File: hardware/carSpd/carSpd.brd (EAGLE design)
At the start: 160 x 100 mm, 0 parts

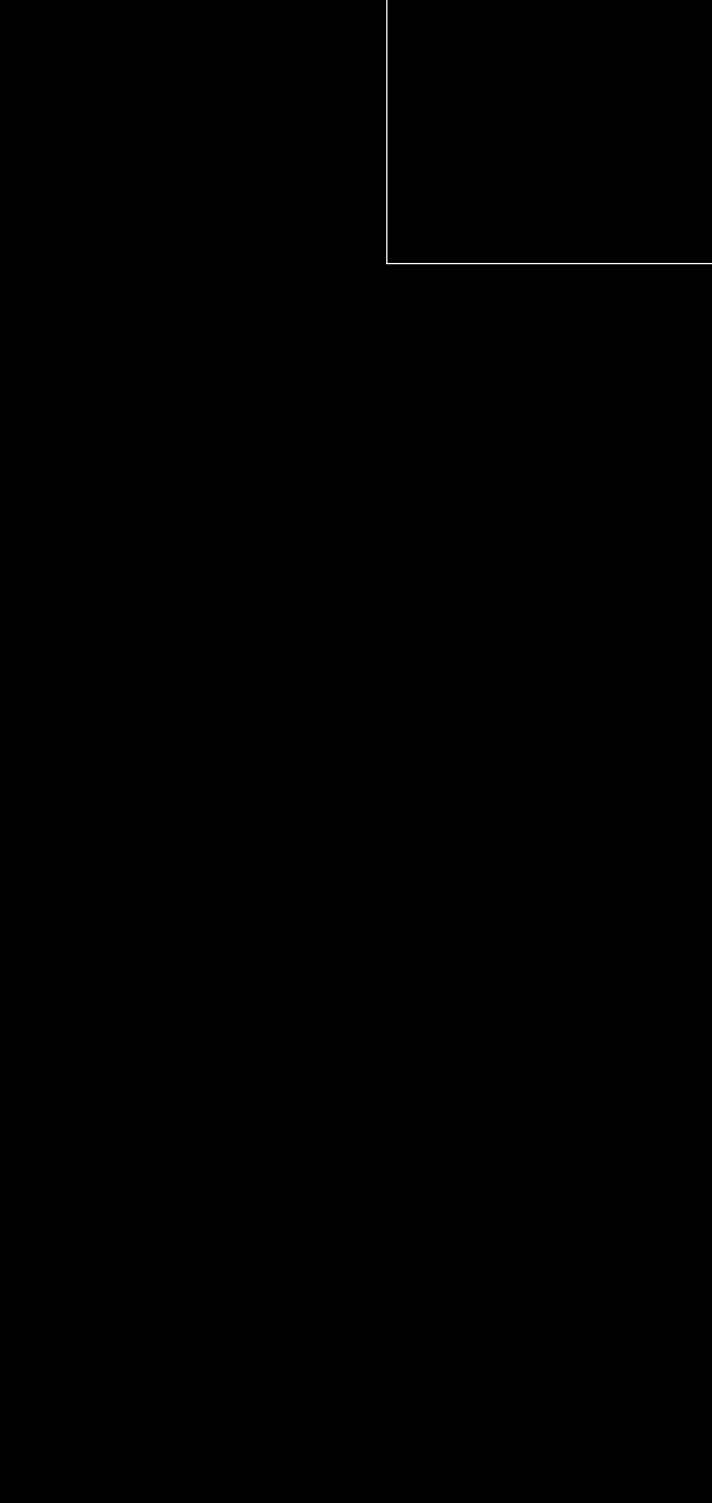
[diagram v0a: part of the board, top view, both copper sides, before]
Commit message: Added power regulator schematics
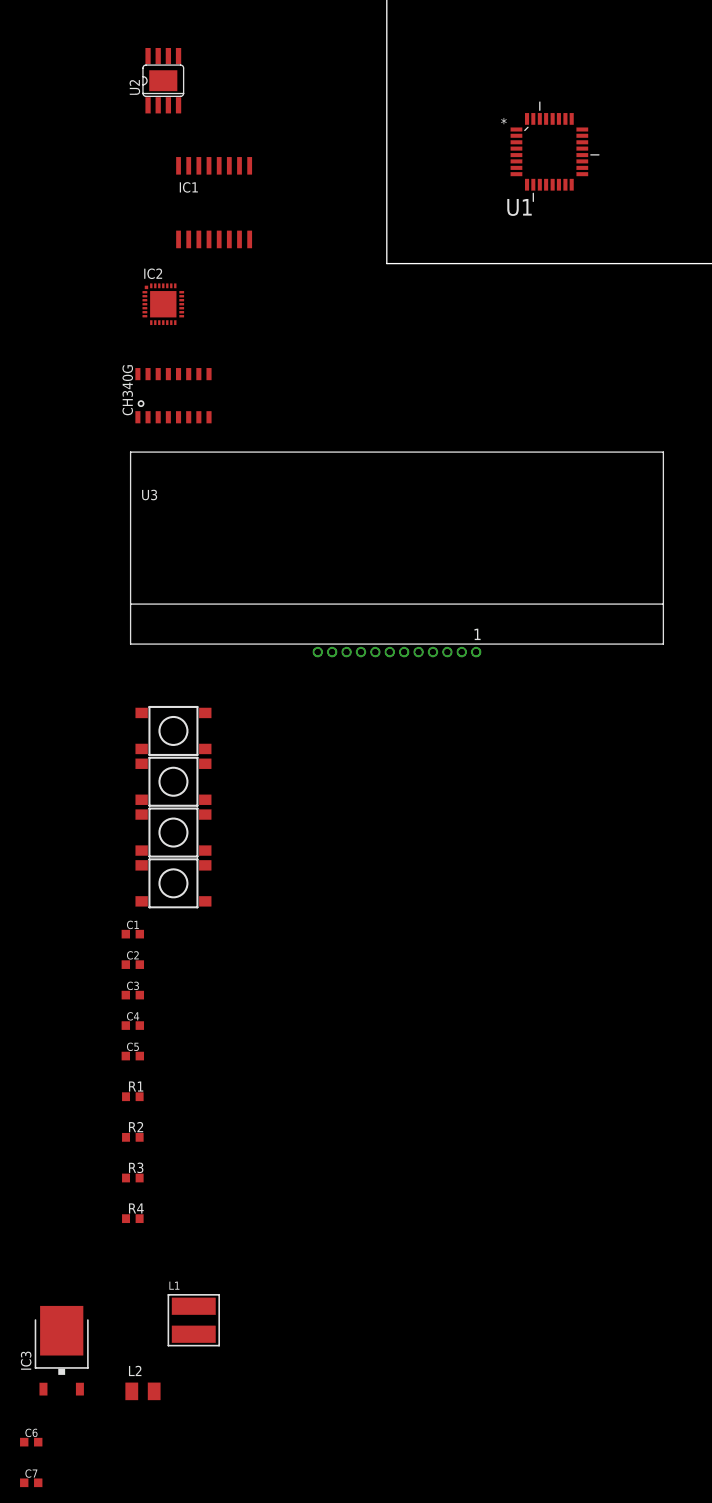
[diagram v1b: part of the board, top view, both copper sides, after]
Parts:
- added C1: 10uf, rcl:C0603K
- added C2: 22uf, rcl:C0603K
- added C3: 3.9nf, rcl:C0603K
- added C4, C7: .1uf, rcl:C0603K
- added C5: 10nf, rcl:C0603K
- added C6: .33uf, rcl:C0603K
- added IC1: DS3231/SO, adafruit:SO16W
- added IC2: CP2102, silabs:MLP28
- added IC3: 7805DT, adafruit:TO252
- added L1: CD54, inductor-sumida:CD54
- added L2: 10uh, rcl:L3225M
- added R1: 10k, rcl:R0603
- added R2: 100k, rcl:R0603
- added R3: 6.8k, rcl:R0603
- added R4: 44.2k, rcl:R0603
- added S1, S2, S3, S4: SWITCH-MOMENTARY-2SMD-4, SparkFun-Electromechanical:TACTILE_SWITCH_TALL
- added U$1: CH340G, ch340g:SOIC16
- added U1: ATMEGA328P-AU, Atmel_By_element14_Batch_1-00:QFP80P900X900X120-32N
- added U2: MP2307, hybridair:SOIC8
- added U3: ERC1602-4, hybridair:ERC1602-4
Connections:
- new net +12V: C1.1, C6.1, IC3.1, R2.2, U2.2
- new net +5V: C2.1, C7.1, IC3.2, L1.1, L2.1, R4.1
- new net AVCC: U1.18
- new net GND: C1.2, C2.2, C4.2, C6.2, C7.2, IC1.13, IC2.3, IC2.EXP, IC2.M, IC3.3, R1.1, R3.1, U2.4, U2.P$1
- new net N$1: C5.2, U2.1
- new net N$2: C5.1, L1.2, L2.2, U2.3
- new net N$3: R1.2, R4.2, U2.5
- new net N$5: C3.2, R3.2
- new net N$6: C3.1, U2.6
- new net N$7: C4.1, U2.8
- new net N$9: R2.1, U2.7
- new net VBAT: IC1.14
- new net VCC: IC1.2, U1.6
- new net VCC_2: U1.4
- new net VDD: IC2.6

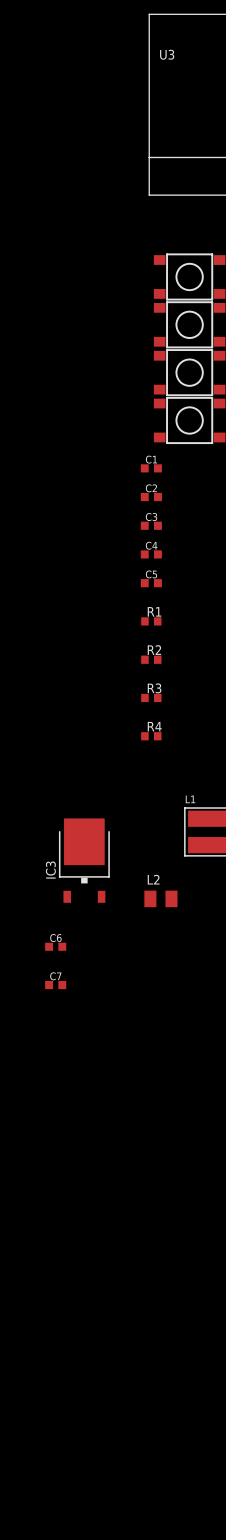
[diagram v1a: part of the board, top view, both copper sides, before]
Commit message: Added USB to serial schematics
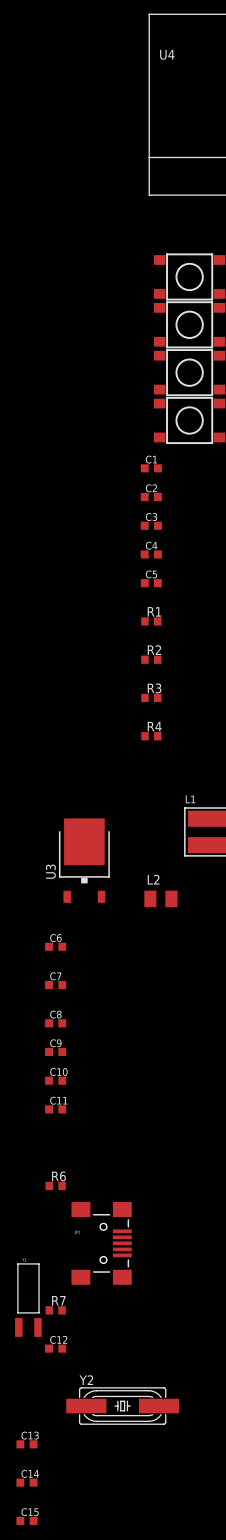
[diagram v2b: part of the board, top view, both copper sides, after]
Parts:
- removed IC3: 7805DT, adafruit:TO252
- added C10, C11, C15, C9: 0.1uf, rcl:C0603K
- added C12: 10nf, rcl:C0603K
- added C13, C14: 18pf, rcl:C0603K
- added C8: 1uf, rcl:C0603K
- added JP1: USBSMD, SparkFun-Connectors:USB-MINIB
- added R6: 4.7k, rcl:R0603
- added R7: 10k, rcl:R0603
- added U4: ERC1602-4, hybridair:ERC1602-4
- added Y1: 12mhz, SparkFun-FreqCtrl:SMD-CYLINDER
- added Y2: (no value), SparkFun-FreqCtrl:HC49UP
- U3: value ERC1602-4 -> 7805DT; device hybridair:ERC1602-4 -> adafruit:TO252
- moved U3 108.7 mm to (-40.6, -135.9)
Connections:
- removed net VDD: IC2.6
- new net D+: IC2.4, U$1.5
- new net D-: IC2.5, U$1.6
- new net N$10: C11.1, IC2.28
- new net N$12: C10.1, IC2.6
- new net N$16: C15.1, U$1.13
- new net N$17: C12.1, U$1.4
- new net N$18: C14.2, U$1.8, Y1.X2, Y2.2
- new net N$19: C13.2, U$1.7, Y1.X1, Y2.1
- new net N$4: IC2.9, R6.1
- new net N$8: IC2.11, R7.2
- new net RST: C11.2, C15.2
- new net RX: IC2.26, U$1.2
- new net TX: IC2.25, U$1.3
- net +12V: now also U3.1; no longer IC3.1
- net +5V: now also C8.1, C9.1, IC2.7, IC2.8, R6.2, U$1.16, U3.2; no longer IC3.2
- net GND: now also C10.2, C12.2, C13.1, C14.1, C8.2, C9.2, R7.1, U$1.1, U3.3; no longer IC3.3
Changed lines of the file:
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@@
 </element>
 <element name="U$1" library="ch340g" package="SOIC16" value="CH340G" x="-26.67" y="-16.51"/>
-<element name="U3" library="hybridair" package="ERC1602-4" value="ERC1602-4" x="1.27" y="-35.56"/>
+<element name="U4" library="hybridair" package="ERC1602-4" value="ERC1602-4" x="1.27" y="-35.56"/>
 <element name="S1" library="SparkFun-Electromechanical" package="TACTILE_SWITCH_TALL" value="SWITCH-MOMENTARY-2SMD-4" x="-26.67" y="-58.42">
 <attribute name="PROD_ID" value="SWCH-11966" x="-26.67" y="-58.42" size="1.778" layer="27" display="off"/>
@@
 <element name="L1" library="inductor-sumida" package="CD54" value="CD54" x="-24.13" y="-132.08"/>
 <element name="L2" library="rcl" package="L3225M" value="10uh" x="-30.48" y="-140.97"/>
-<element name="IC3" library="adafruit" package="TO252" value="7805DT" x="-40.64" y="-135.89"/>
+<element name="U3" library="adafruit" package="TO252" value="7805DT" x="-40.64" y="-135.89"/>
 <element name="C6" library="rcl" package="C0603K" value=".33uf" x="-44.45" y="-147.32"/>
 <element name="C7" library="rcl" package="C0603K" value=".1uf" x="-44.45" y="-152.4"/>
+<element name="C8" library="rcl" package="C0603K" value="1uf" x="-44.45" y="-157.48"/>
+<element name="C9" library="rcl" package="C0603K" value="0.1uf" x="-44.45" y="-161.29"/>
+<element name="C10" library="rcl" package="C0603K" value="0.1uf" x="-44.45" y="-165.1"/>
+<element name="C11" library="rcl" package="C0603K" value="0.1uf" x="-44.45" y="-168.91"/>
+<element name="R6" library="rcl" package="R0603" value="4.7k" x="-44.45" y="-179.07"/>
+<element name="JP1" library="SparkFun-Connectors" package="USB-MINIB" value="USBSMD" x="-38.1" y="-186.69">
+<attribute name="PROD_ID" value="CONN-08193" x="-38.1" y="-186.69" size="1.778" layer="27" display="off"/>
+</element>
+<element name="R7" library="rcl" package="R0603" value="10k" x="-44.45" y="-195.58"/>
+<element name="C12" library="rcl" package="C0603K" value="10nf" x="-44.45" y="-200.66"/>
+<element name="Y1" library="SparkFun-FreqCtrl" package="SMD-CYLINDER" value="12mhz" x="-48.26" y="-198.12"/>
+<element name="Y2" library="SparkFun-FreqCtrl" package="HC49UP" value="" x="-35.56" y="-208.28"/>
+<element name="C13" library="rcl" package="C0603K" value="18pf" x="-48.26" y="-213.36"/>
+<element name="C14" library="rcl" package="C0603K" value="18pf" x="-48.26" y="-218.44"/>
+<element name="C15" library="rcl" package="C0603K" value="0.1uf" x="-48.26" y="-223.52"/>
 </elements>
 <signals>
@@
 <signal name="GND">
 <contactref element="IC1" pad="13"/>
-<contactref element="IC2" pad="3"/>
-<contactref element="IC2" pad="EXP"/>
-<contactref element="IC2" pad="M"/>
 <contactref element="U2" pad="P$1"/>
 <contactref element="U2" pad="4"/>
@@
 <contactref element="C4" pad="2"/>
 <contactref element="C6" pad="2"/>
-<contactref element="IC3" pad="3"/>
+<contactref element="U3" pad="3"/>
 <contactref element="C7" pad="2"/>
+<contactref element="R7" pad="1"/>
+<contactref element="IC2" pad="3"/>
+<contactref element="IC2" pad="EXP"/>
+<contactref element="IC2" pad="M"/>
+<contactref element="C10" pad="2"/>
+<contactref element="C9" pad="2"/>
+<contactref element="C8" pad="2"/>
+<contactref element="U$1" pad="1"/>
+<contactref element="C12" pad="2"/>
+<contactref element="C13" pad="1"/>
+<contactref element="C14" pad="1"/>
+<wire x1="-45.3" y1="-195.58" x2="-43.575" y2="-200.66" width="0" layer="19" extent="1-1"/>
+<wire x1="-49.135" y1="-213.36" x2="-43.575" y2="-200.66" width="0" layer="19" extent="1-1"/>
+<wire x1="-49.135" y1="-218.44" x2="-49.135" y2="-213.36" width="0" layer="19" extent="1-1"/>
+<wire x1="-43.575" y1="-165.1" x2="-45.3" y2="-195.58" width="0" layer="19" extent="1-1"/>
+<wire x1="-43.575" y1="-161.29" x2="-43.575" y2="-165.1" width="0" layer="19" extent="1-1"/>
+<wire x1="-43.575" y1="-157.48" x2="-43.575" y2="-161.29" width="0" layer="19" extent="1-1"/>
+<wire x1="-43.575" y1="-152.4" x2="-43.575" y2="-157.48" width="0" layer="19" extent="1-1"/>
 <wire x1="-43.575" y1="-147.32" x2="-43.575" y2="-152.4" width="0" layer="19" extent="1-1"/>
 <wire x1="-40.64" y1="-133.39" x2="-43.575" y2="-147.32" width="0" layer="19" extent="1-1"/>
@@
 <wire x1="-30.875" y1="-87.63" x2="-30.875" y2="-95.25" width="0" layer="19" extent="1-1"/>
 <wire x1="-30.875" y1="-83.82" x2="-30.875" y2="-87.63" width="0" layer="19" extent="1-1"/>
-<wire x1="-27.94" y1="-5.08" x2="-30.875" y2="-83.82" width="0" layer="19" extent="1-1"/>
+<wire x1="-31.115" y1="-19.205" x2="-30.875" y2="-83.82" width="0" layer="19" extent="1-1"/>
+<wire x1="-27.94" y1="-5.08" x2="-31.115" y2="-19.205" width="0" layer="19" extent="1-1"/>
 <wire x1="-30.24" y1="-4.58" x2="-27.94" y2="-5.08" width="0" layer="19" extent="1-1"/>
 <wire x1="-30.0425" y1="-2.9775" x2="-30.24" y2="-4.58" width="0" layer="19" extent="1-1"/>
@@
 <wire x1="-26.035" y1="19.7866" x2="-22.225" y2="12.22" width="0" layer="19" extent="1-1"/>
 <wire x1="-27.94" y1="22.86" x2="-26.035" y2="19.7866" width="0" layer="19" extent="1-1"/>
-</signal>
-<signal name="VDD">
-<contactref element="IC2" pad="6"/>
 </signal>
 <signal name="N$1">
@@
 <contactref element="R4" pad="1"/>
 <contactref element="C7" pad="1"/>
-<contactref element="IC3" pad="2"/>
+<contactref element="U3" pad="2"/>
+<contactref element="R6" pad="2"/>
+<contactref element="IC2" pad="8"/>
+<contactref element="IC2" pad="7"/>
+<contactref element="C9" pad="1"/>
+<contactref element="C8" pad="1"/>
+<contactref element="U$1" pad="16"/>
+<wire x1="-45.325" y1="-161.29" x2="-43.6" y2="-179.07" width="0" layer="19" extent="1-1"/>
+<wire x1="-45.325" y1="-157.48" x2="-45.325" y2="-161.29" width="0" layer="19" extent="1-1"/>
+<wire x1="-45.325" y1="-152.4" x2="-45.325" y2="-157.48" width="0" layer="19" extent="1-1"/>
 <wire x1="-38.36" y1="-140.69" x2="-45.325" y2="-152.4" width="0" layer="19" extent="1-1"/>
 <wire x1="-31.88" y1="-140.97" x2="-38.36" y2="-140.69" width="0" layer="19" extent="1-1"/>
@@
 <wire x1="-32.6" y1="-119.38" x2="-24.13" y2="-130.33" width="0" layer="19" extent="1-1"/>
 <wire x1="-32.625" y1="-87.63" x2="-32.6" y2="-119.38" width="0" layer="19" extent="1-1"/>
+<wire x1="-31.115" y1="-13.815" x2="-32.625" y2="-87.63" width="0" layer="19" extent="1-1"/>
+<wire x1="-29.44" y1="-7.38" x2="-31.115" y2="-13.815" width="0" layer="19" extent="1-1"/>
+<wire x1="-30.24" y1="-6.58" x2="-29.44" y2="-7.38" width="0" layer="19" extent="1-1"/>
 </signal>
 <signal name="+12V">
@@
 <contactref element="R2" pad="2"/>
 <contactref element="C6" pad="1"/>
-<contactref element="IC3" pad="1"/>
+<contactref element="U3" pad="1"/>
 <wire x1="-42.92" y1="-140.69" x2="-45.325" y2="-147.32" width="0" layer="19" extent="1-1"/>
 <wire x1="-30.9" y1="-109.22" x2="-42.92" y2="-140.69" width="0" layer="19" extent="1-1"/>
@@
 <wire x1="-28.575" y1="25.9334" x2="-32.6" y2="-109.22" width="0" layer="19" extent="1-1"/>
 </signal>
+<signal name="N$4">
+<contactref element="IC2" pad="9"/>
+<contactref element="R6" pad="1"/>
+<wire x1="-28.94" y1="-7.38" x2="-45.3" y2="-179.07" width="0" layer="19" extent="1-1"/>
+</signal>
+<signal name="N$8">
+<contactref element="R7" pad="2"/>
+<contactref element="IC2" pad="11"/>
+<wire x1="-27.94" y1="-7.38" x2="-43.6" y2="-195.58" width="0" layer="19" extent="1-1"/>
+</signal>
+<signal name="N$10">
+<contactref element="IC2" pad="28"/>
+<contactref element="C11" pad="1"/>
+<wire x1="-29.44" y1="-2.78" x2="-45.325" y2="-168.91" width="0" layer="19" extent="1-1"/>
+</signal>
+<signal name="RST">
+<contactref element="C11" pad="2"/>
+<contactref element="C15" pad="2"/>
+<wire x1="-47.385" y1="-223.52" x2="-43.575" y2="-168.91" width="0" layer="19" extent="1-1"/>
+</signal>
+<signal name="RX">
+<contactref element="IC2" pad="26"/>
+<contactref element="U$1" pad="2"/>
+<wire x1="-28.44" y1="-2.78" x2="-29.845" y2="-19.205" width="0" layer="19" extent="1-1"/>
+</signal>
+<signal name="TX">
+<contactref element="IC2" pad="25"/>
+<contactref element="U$1" pad="3"/>
+<wire x1="-27.94" y1="-2.78" x2="-28.575" y2="-19.205" width="0" layer="19" extent="1-1"/>
+</signal>
+<signal name="N$12">
+<contactref element="IC2" pad="6"/>
+<contactref element="C10" pad="1"/>
+<wire x1="-30.24" y1="-6.08" x2="-45.325" y2="-165.1" width="0" layer="19" extent="1-1"/>
+</signal>
+<signal name="D+">
+<contactref element="IC2" pad="4"/>
+<contactref element="U$1" pad="5"/>
+<wire x1="-30.24" y1="-5.08" x2="-26.035" y2="-19.205" width="0" layer="19" extent="1-1"/>
+</signal>
+<signal name="D-">
+<contactref element="IC2" pad="5"/>
+<contactref element="U$1" pad="6"/>
+<wire x1="-30.24" y1="-5.58" x2="-24.765" y2="-19.205" width="0" layer="19" extent="1-1"/>
+</signal>
+<signal name="N$17">
+<contactref element="U$1" pad="4"/>
+<contactref element="C12" pad="1"/>
+<wire x1="-27.305" y1="-19.205" x2="-45.325" y2="-200.66" width="0" layer="19" extent="1-1"/>
+</signal>
+<signal name="N$18">
+<contactref element="Y2" pad="2"/>
+<contactref element="Y1" pad="X2"/>
+<contactref element="U$1" pad="8"/>
+<contactref element="C14" pad="2"/>
+<wire x1="-30.734" y1="-208.28" x2="-46.8" y2="-197.85" width="0" layer="19" extent="1-1"/>
+<wire x1="-47.385" y1="-218.44" x2="-30.734" y2="-208.28" width="0" layer="19" extent="1-1"/>
+<wire x1="-22.225" y1="-19.205" x2="-46.8" y2="-197.85" width="0" layer="19" extent="1-1"/>
+</signal>
+<signal name="N$19">
+<contactref element="U$1" pad="7"/>
+<contactref element="Y1" pad="X1"/>
+<contactref element="Y2" pad="1"/>
+<contactref element="C13" pad="2"/>
+<wire x1="-47.385" y1="-213.36" x2="-40.386" y2="-208.28" width="0" layer="19" extent="1-1"/>
+<wire x1="-49.34" y1="-197.85" x2="-40.386" y2="-208.28" width="0" layer="19" extent="1-1"/>
+<wire x1="-23.495" y1="-19.205" x2="-49.34" y2="-197.85" width="0" layer="19" extent="1-1"/>
+</signal>
+<signal name="N$16">
+<contactref element="U$1" pad="13"/>
+<contactref element="C15" pad="1"/>
+<wire x1="-49.135" y1="-223.52" x2="-27.305" y2="-13.815" width="0" layer="19" extent="1-1"/>
+</signal>
 </signals>

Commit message: Added peripheral schematics
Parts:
- added B1: BATTERY1220, Battery&Holder:1220-SMD
- added C16, C20: 0.1uf, rcl:C0603K
- added C17, C19: 1uf, rcl:C0603K
- added C18: 10uf, rcl:C0603K
- added DISP_LED: (no value), SparkFun-Connectors:1X02_NO_SILK
- added LED1, LED2, LED3, LED4: (no value), led:CHIPLED_0805
- added Q1: 2n3904, SparkFun-DiscreteSemi:SOT23-3
- added R10, R9: 4.7k, rcl:R0603
- added R5: 10k, rcl:R0603
- added R8: 220, rcl:R0603
- added U$2: DS1820, Ava:µSOP8
- renumbered U4 to DISPLAY
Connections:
- removed net VBAT: IC1.14
- new net LED_PWM: R5.2
- new net N$11: Q1.1, R5.1
- new net N$13: DISP_LED.2, R8.1
- new net N$14: C17.2, DISPLAY.8
- new net N$15: Q1.3, R8.2, R9.2
- new net N$20: C19.1, DISPLAY.11
- new net N$21: C19.2, DISPLAY.12
- new net N$23: LED1.A, LED2.A, LED3.A, LED4.A, R9.1
- new net N$27: B1.+, IC1.14
- new net SCL: DISPLAY.4, IC1.16
- new net SDA: DISPLAY.5, IC1.15
- new net TEMP: R10.1, U$2.1
- net +5V: now also C16.1, C17.1, C18.1, C20.1, DISPLAY.1, DISPLAY.2, DISPLAY.7, DISPLAY.9, IC1.2, R10.2, U$2.8
- net GND: now also B1.-, C16.2, C18.2, C20.2, DISPLAY.10, DISPLAY.3, DISPLAY.6, DISP_LED.1, IC1.10, IC1.11, IC1.12, IC1.5, IC1.6, IC1.7, IC1.8, IC1.9, LED1.C, LED2.C, LED3.C, LED4.C, Q1.2, U$2.4
- net VCC: no longer IC1.2

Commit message: Finished schematic, unverified
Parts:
- removed U1: ATMEGA328P-AU, Atmel_By_element14_Batch_1-00:QFP80P900X900X120-32N
- added C22, C23: 18pf, rcl:C0603K
- added C24, C25: 0.1uf, rcl:C0603K
- added D1, D2, D3: 5.1V, SparkFun-DiscreteSemi:SOD-323
- added JP2: AVR_ICSP, SparkFun-Connectors:2X3_TEST_POINTS
- added JP3: USBSMD, SparkFun-Connectors:USB-MINIB
- added LED5: STATUS, led:CHIPLED_0805
- added LED6: POWER, led:CHIPLED_0805
- added R11: 10k, rcl:R0603
- added R12, R13: 4.7k, rcl:R0603
- added R14: 220, rcl:R0603
- added R15, R16, R17: 50k, rcl:R0603
- added R18: 1k, rcl:R0603
- added S5: RESET, SparkFun-Electromechanical:TACTILE-SWITCH-1101NE
- added U$3, U$4, U$5: 5.1V, hybridair:SOD-80
- added U4: ATMEGA328P_TQFP, SparkFun-DigitalIC:TQFP32-08
- added Y3: 16mhz, SparkFun-FreqCtrl:HC49UP
- JP1: value USBSMD -> CAR_INPUT; device SparkFun-Connectors:USB-MINIB -> SparkFun-Connectors:1X05
- S1, S2, S3, S4: value SWITCH-MOMENTARY-2SMD-4 -> (none)
- moved JP1 286.4 mm to (-95.2, -467.4)
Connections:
- removed net AVCC: U1.18
- removed net VCC: U1.6
- removed net VCC_2: U1.4
- new net INJ: JP1.3, R15.1
- new net LIGHTING: JP1.4, R17.1
- new net N$22: JP2.1, U4.16
- new net N$24: C22.1, U4.7, Y3.2
- new net N$26: JP2.3, LED5.A, U4.17
- new net N$28: S1.A2, U4.10
- new net N$29: LED6.A, R18.1
- new net N$30: D2.C, R15.2, U$4.C, U4.1, U4.32
- new net N$31: D1.C, R17.2, U$3.C, U4.23
- new net N$32: LED5.C, R14.1
- new net N$33: S3.A2, U4.12
- new net N$34: S2.A2, U4.11
- new net N$35: S4.A2, U4.13
- new net N$36: D3.C, R16.2, U$5.C, U4.9
- new net N$37: C23.1, U4.8, Y3.1
- new net VSS: JP1.2, R16.1
- net +12V: now also JP1.1
- net +5V: now also C24.1, C25.1, JP2.2, JP3.VBUS, R11.1, R12.1, R13.1, R18.2, U4.18, U4.4, U4.6
- net D+: now also JP3.D+
- net D-: now also JP3.D-
- net GND: now also C22.2, C23.2, C24.2, C25.2, D1.A, D2.A, D3.A, JP1.5, JP2.6, JP3.GND, LED6.C, R14.2, S1.B2, S2.B2, S3.B2, S4.B2, S5.1, U$3.A, U$4.A, U$5.A, U4.21, U4.3, U4.5
- net LED_PWM: now also JP2.4, U4.15
- net RST: now also JP2.5, R11.2, S5.2, U4.29
- net RX: now also U4.30
- net SCL: now also R13.2, U4.28
- net SDA: now also R12.2, U4.27
- net TX: now also U4.31
